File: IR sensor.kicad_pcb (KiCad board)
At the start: 2 copper layers, 33.5 x 16.8 mm, 23 parts, among them P1 BNC, P2 BNC, P3 BNC, P4 CONN_01X02, Q1 SOT-23-3 NPN, U1 TLV2770IDGKR, U2 LM311MX/NOPB

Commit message: ENH: Updates to IR sensors
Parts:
- removed D1: LED, Pin_Headers:Pin_Header_Straight_1x02
- removed P3: BNC, Pin_Headers:Pin_Header_Straight_1x02
- removed P4: CONN_01X02, Pin_Headers:Pin_Header_Straight_1x02
- removed the REF** at (142.0, 67.3)
- removed the REF** at (169.9, 78.5)
- removed RV1: POT, Pin_Headers:Pin_Header_Straight_1x03
- added REF**: 1pin, Connect:1pin, F.Cu at (172.2, 72.6)
- added REF**: 1pin, Connect:1pin, F.Cu at (140.7, 72.6)
- P1: value BNC -> CONN_01X08; footprint Pin_Headers:Pin_Header_Straight_1x02 -> Terminal_Blocks:TerminalBlock_Pheonix_MPT-2.54mm_8pol; moved to B.Cu
- P2: value BNC -> CONN_01X07; footprint Pin_Headers:Pin_Header_Straight_1x02 -> Terminal_Blocks:TerminalBlock_Pheonix_MPT-2.54mm_7pol; moved to B.Cu
- U1: value TLV2770IDGKR -> TLV2770
- U2: value LM311MX/NOPB -> LM311
- moved C1 12.3 mm to (165.4, 67.3), turned to 180 degrees
- moved P2 11.9 mm to (145.8, 67.1), turned to 0 degrees
- moved P1 9.40 mm to (163.6, 78.7), turned to 180 degrees
- moved R7 5.95 mm to (162.1, 75.7), turned to 0 degrees
- moved C5 4.36 mm to (164.5, 69.5), turned to 180 degrees
- moved R6 2.75 mm to (163.8, 72.9), turned to 90 degrees
- moved R1 2.54 mm to (157.2, 75.7), turned to 0 degrees
- moved Q1 1.83 mm to (166.4, 73.7), turned to 0 degrees
- moved R5 1.05 mm to (164.1, 71.1), turned to 180 degrees
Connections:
- C3 pad 1: Net-(C3-Pad1) -> IR+
- P1 pad 1: Net-(P1-Pad1) -> GND
- P1 pad 2: GND -> TTL+
- P2 pad 1: Net-(P2-Pad1) -> GND
- P2 pad 2: GND -> LED+
- Q1 pad 3: Net-(D1-Pad2) -> LED+
- R1 pad 2: Net-(P1-Pad1) -> E+
- R2 pad 2: Net-(P2-Pad1) -> S+
- R3 pad 2: Net-(P2-Pad1) -> S+
- R5 pad 2: Net-(P3-Pad1) -> TTL+
- R6 pad 2: Net-(P3-Pad1) -> TTL+
- U1 pad 2: Net-(C3-Pad1) -> IR+
- U1 pad 6: Net-(C3-Pad1) -> IR+
- U2 pad 2: Net-(C3-Pad1) -> IR+
- U2 pad 3: Net-(RV1-Pad2) -> POT2
- U2 pad 7: Net-(P3-Pad1) -> TTL+
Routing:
- net LED+: track 0.00 -> 27.9 mm
- net IR+: track 0.00 -> 23.4 mm
- net Net-(P3-Pad1): track 15.4 -> 0.00 mm
- net Net-(RV1-Pad2): track 13.6 -> 0.00 mm
- net TTL+: track 0.00 -> 12.1 mm
- net Net-(C3-Pad1): track 11.5 -> 0.00 mm
- net Net-(D1-Pad2): track 11.4 -> 0.00 mm
- net POT2: track 0.00 -> 10.7 mm
- net +5V: track 57.9 -> 49.6 mm
- net Net-(P2-Pad1): track 6.95 -> 0.00 mm
- net S+: track 0.00 -> 4.53 mm
- net E+: track 0.00 -> 4.03 mm
- net Net-(P1-Pad1): track 3.44 -> 0.00 mm
- net Net-(Q1-Pad2): track 2.16 -> 4.03 mm
- net Net-(Q1-Pad1): track 1.80 -> 2.35 mm
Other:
- board size 33.5 x 16.8 mm -> 36.6 x 16.8 mm
- board text added: "5V"
- board text added: "LED"
- board text added: "P1"
- board text added: "P2"
- board text added: "P3"
- board text removed: "POT"
- board text removed: "PWR"

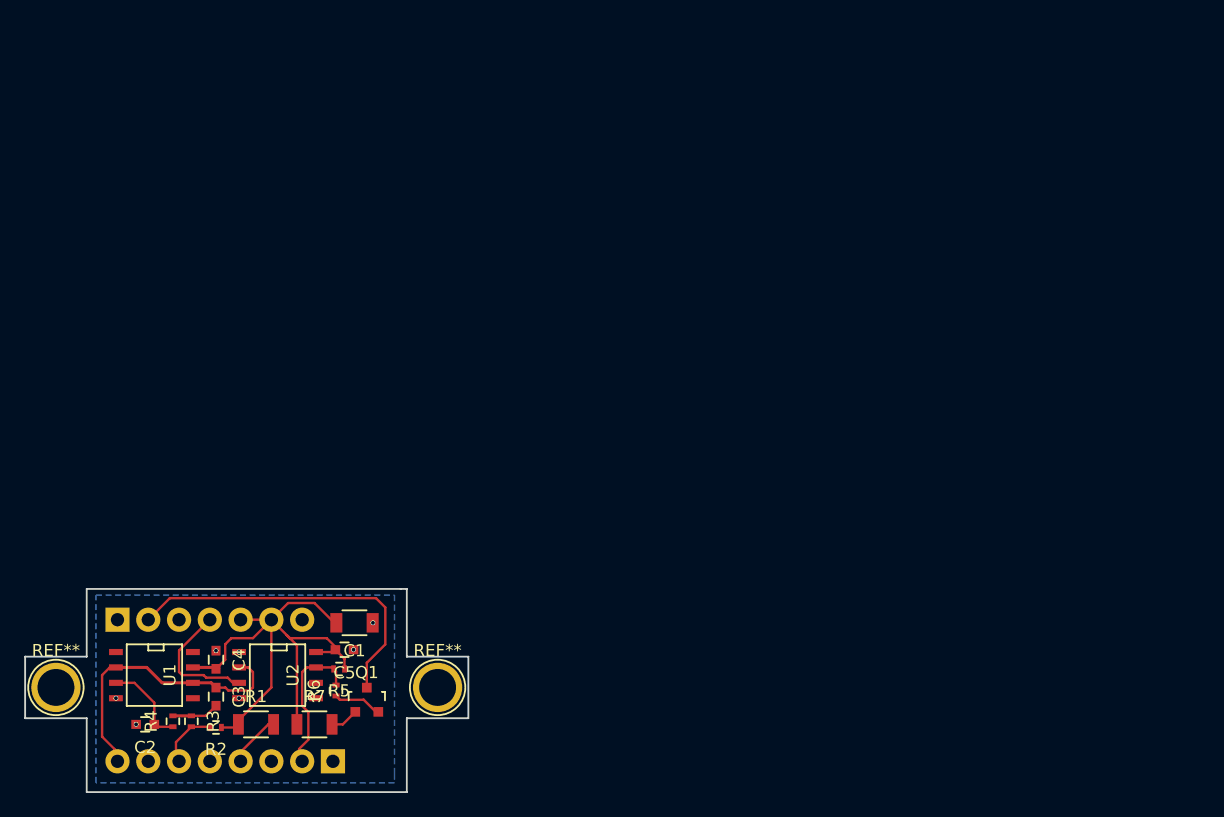
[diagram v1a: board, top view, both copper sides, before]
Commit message: ENH: Make PCB more compact
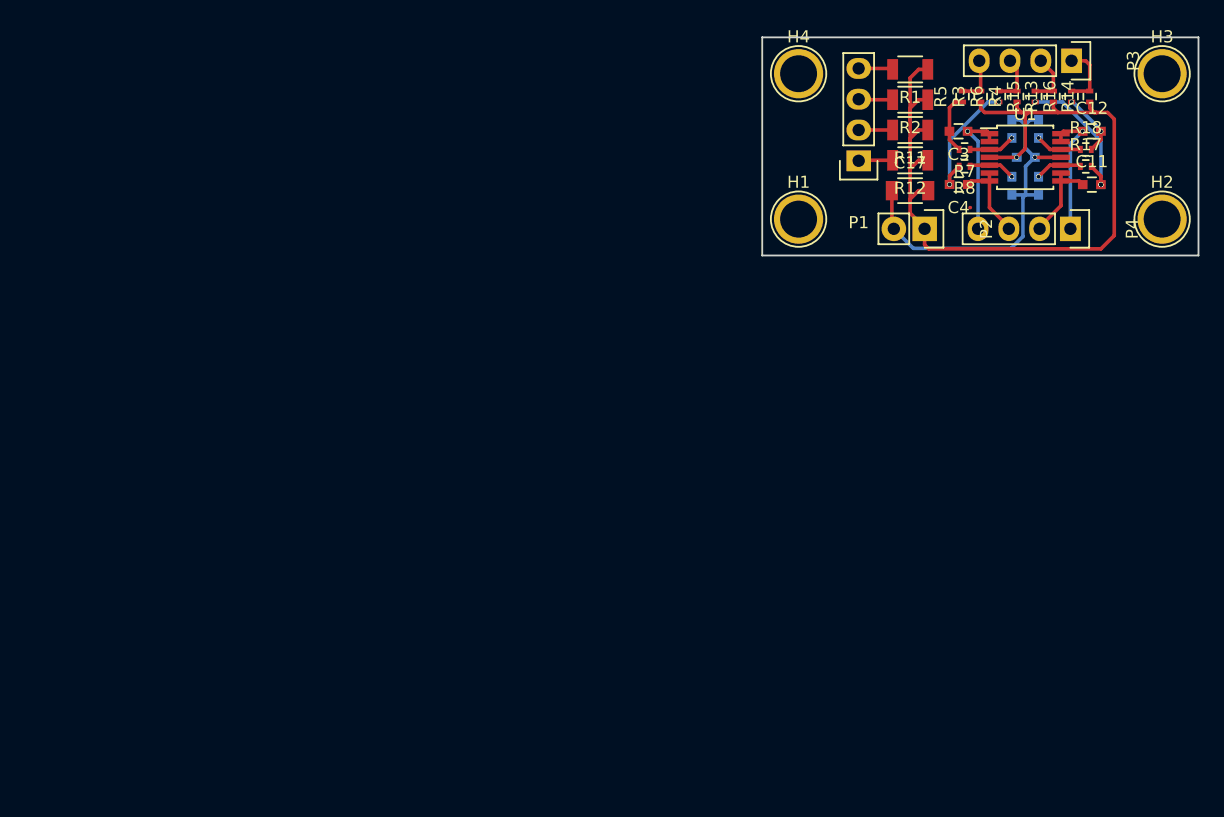
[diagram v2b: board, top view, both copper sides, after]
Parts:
- removed Q1: SOT-23-3 NPN, TO_SOT_Packages_SMD:SOT-23
- removed REF** (x2): 1pin, Connect:1pin
- removed U2: LM311, SMD_Packages:SOIC-8-N
- added C10: 0.1uF, Capacitors_SMD:C_0603, B.Cu at (221.8, 26.6)
- added C11: 0.1uF, Capacitors_SMD:C_0603, F.Cu at (226.2, 31.1)
- added C12: 0.1uF, Capacitors_SMD:C_0603, F.Cu at (226.2, 26.8)
- added C17: 10uF, Capacitors_SMD:C_1206, F.Cu at (211.2, 31.6)
- added C9: 0.1uF, Capacitors_SMD:C_0603, B.Cu at (221.8, 31.2)
- added H1: CONN_01X01, Connect:1pin, F.Cu at (202.0, 34.0)
- added H2: CONN_01X01, Connect:1pin, F.Cu at (232.0, 34.0)
- added H3: CONN_01X01, Connect:1pin, F.Cu at (232.0, 22.0)
- added H4: CONN_01X01, Connect:1pin, F.Cu at (202.0, 22.0)
- added P3: CONN_01X04, Pin_Headers:Pin_Header_Straight_1x04, F.Cu at (224.5, 20.9)
- added P4: CONN_01X04, Pin_Headers:Pin_Header_Straight_1x04, F.Cu at (224.4, 34.8)
- added R11: 100 0.25W, Resistors_SMD:R_1206, F.Cu at (211.2, 26.6)
- added R12: 100 0.25W, Resistors_SMD:R_1206, F.Cu at (211.2, 29.1)
- added R13: 10k, Resistors_SMD:R_0402, F.Cu at (223.0, 23.9)
- added R14: 10k, Resistors_SMD:R_0402, F.Cu at (226.0, 23.9)
- added R15: 10k, Resistors_SMD:R_0402, F.Cu at (221.5, 23.9)
- added R16: 10k, Resistors_SMD:R_0402, F.Cu at (224.5, 23.9)
- added R17: 10k, Resistors_SMD:R_0402, F.Cu at (225.7, 29.6)
- added R18: 10k, Resistors_SMD:R_0402, F.Cu at (225.7, 28.2)
- added R8: 10k, Resistors_SMD:R_0402, F.Cu at (215.7, 29.6)
- C1: value 10uF -> 0.1uF; footprint Capacitors_SMD:C_1206 -> Capacitors_SMD:C_0603; moved to B.Cu
- C2, C5: moved to B.Cu
- P1: value CONN_01X08 -> CONN_01X04; footprint Terminal_Blocks:TerminalBlock_Pheonix_MPT-2.54mm_8pol -> Pin_Headers:Pin_Header_Straight_1x04; moved to F.Cu
- P2: value CONN_01X07 -> CONN_01X02; footprint Terminal_Blocks:TerminalBlock_Pheonix_MPT-2.54mm_7pol -> Pin_Headers:Pin_Header_Straight_1x02; moved to F.Cu
- R2: value 10k -> 100 0.25W; footprint Resistors_SMD:R_0402 -> Resistors_SMD:R_1206
- R5: value 1k -> 10k
- R6: value 100k -> 10k
- R7: value 100 0.25W -> 10k; footprint Resistors_SMD:R_1206 -> Resistors_SMD:R_0402
- U1: value TLV2770 -> TLV2774; footprint SMD_Packages:SOIC-8-N -> Housings_SSOP:TSSOP-14_4.4x5mm_Pitch0.65mm
- moved R4 86.7 mm to (220.0, 23.9)
- moved C2 84.2 mm to (219.6, 31.2), turned to 270 degrees
- moved U1 83.6 mm to (220.7, 28.9), turned to 0 degrees
- moved R3 83.1 mm to (217.0, 23.9), turned to 90 degrees
- moved R2 77.2 mm to (211.2, 24.1)
- moved C3 77.0 mm to (215.2, 26.8), turned to 180 degrees
- moved R1 76.4 mm to (211.2, 21.6), turned to 180 degrees
- moved P2 74.0 mm to (212.4, 34.8), turned to 270 degrees
- moved R6 73.4 mm to (218.5, 23.9)
- moved C4 72.8 mm to (215.2, 31.1), turned to 180 degrees
- moved R7 71.6 mm to (215.7, 28.2), turned to 180 degrees
- moved R5 69.8 mm to (215.5, 23.9), turned to 90 degrees
- moved C5 69.4 mm to (220.8, 28.9)
- moved C1 67.9 mm to (219.6, 26.6), turned to 90 degrees
- moved P1 65.9 mm to (207.0, 29.2)
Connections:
- net E+ renamed E1+
- C1 pad 1: GND -> Net-(C1-Pad1)
- C1 pad 2: +5V -> GND
- C3 pad 1: IR+ -> O1
- C4 pad 1: GND -> O2
- C4 pad 2: +5V -> Net-(C4-Pad2)
- P1 pad 1: GND -> E4+
- P1 pad 2: TTL+ -> E3+
- P1 pad 3: GND -> E2+
- P2 pad 1: GND -> +5V
- P2 pad 2: LED+ -> GND
- R2 pad 2: S+ -> E2+
- R3 pad 1: Net-(C3-Pad2) -> +5V
- R3 pad 2: S+ -> S1+
- R4 pad 1: Net-(C2-Pad1) -> +5V
- R4 pad 2: Net-(C3-Pad2) -> S2+
- R5 pad 1: +5V -> Net-(C3-Pad2)
- R5 pad 2: TTL+ -> S1+
- R6 pad 1: Net-(Q1-Pad2) -> Net-(C4-Pad2)
- R6 pad 2: TTL+ -> S2+
- R7 pad 1: +5V -> Net-(C1-Pad1)
- R7 pad 2: Net-(Q1-Pad1) -> Net-(C3-Pad2)
- U1 pad 1: (no net) -> O1
- U1 pad 2: IR+ -> O1
- U1 pad 3: Net-(C2-Pad1) -> Net-(C1-Pad1)
- U1 pad 4: GND -> +5V
- U1 pad 5: (no net) -> Net-(C2-Pad1)
- U1 pad 6: IR+ -> O2
- U1 pad 7: +5V -> O2
- U1 pad 8: (no net) -> O3
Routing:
- net GND: track 0.32 -> 31.8 mm, vias 7 -> 1
- net LED+: track 27.9 -> 0.00 mm
- net IR+: track 23.4 -> 0.00 mm
- net +5V: track 49.6 -> 72.2 mm, vias 0 -> 1
- net Net-(C11-Pad2): track 0.00 -> 12.2 mm, vias 0 -> 3
- net TTL+: track 12.1 -> 0.00 mm
- net O4: track 0.00 -> 11.0 mm, vias 0 -> 1
- net O1: track 0.00 -> 11.0 mm, vias 0 -> 1
- net Net-(C4-Pad2): track 0.00 -> 10.8 mm, vias 0 -> 2
- net POT2: track 10.7 -> 0.00 mm
- net O3: track 0.00 -> 7.28 mm
- net O2: track 0.00 -> 7.17 mm
- net Net-(C12-Pad2): track 0.00 -> 5.31 mm, vias 0 -> 2
- net S4+: track 0.00 -> 5.30 mm
- net S+: track 4.53 -> 0.00 mm
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- removed copper zone on B.Cu, net GND
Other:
- board size 36.6 x 16.8 mm -> 36 x 18 mm
- net class Default: clearance 0.2 -> 0.15; trace_width 0.2 -> 0.3
- rule trace_clearance: 0.2 -> 0.15
- board text removed: "5V"
- board text removed: "E"
- board text removed: "IR"
- board text removed: "LED"
- board text removed: "P1"
- board text removed: "P2"
- board text removed: "P3"
- board text removed: "S"
- board text removed: "TTL"
- board text removed: "⏚"

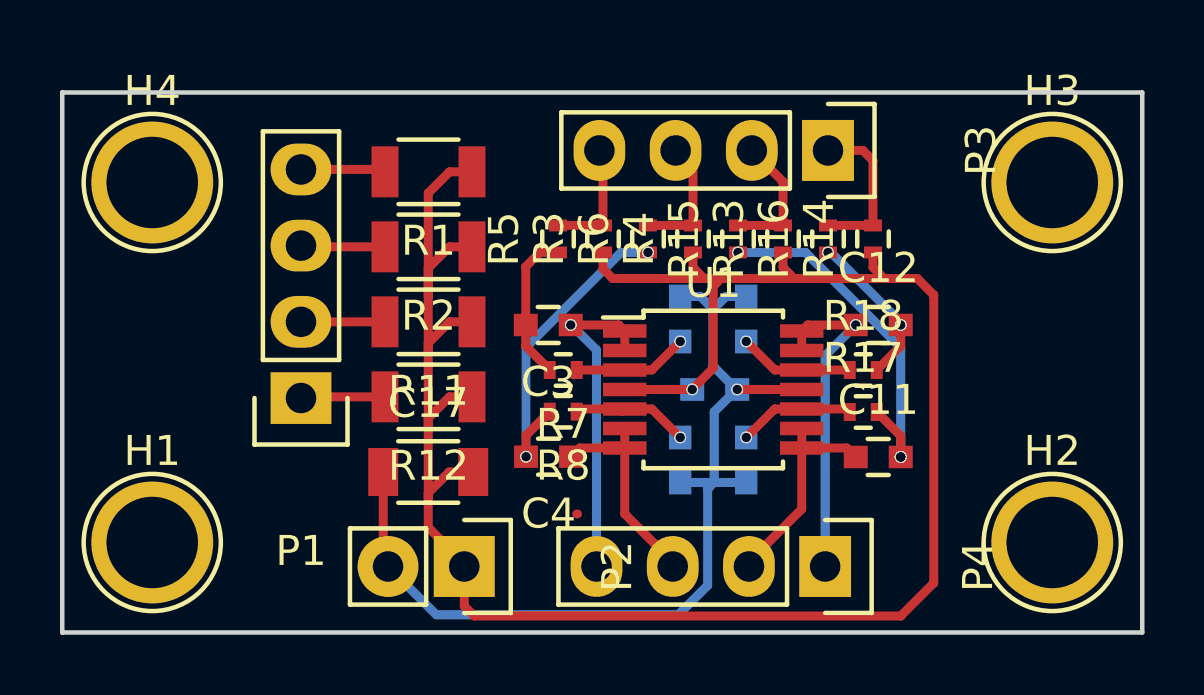
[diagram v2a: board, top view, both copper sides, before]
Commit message: Update to KiCAD 5
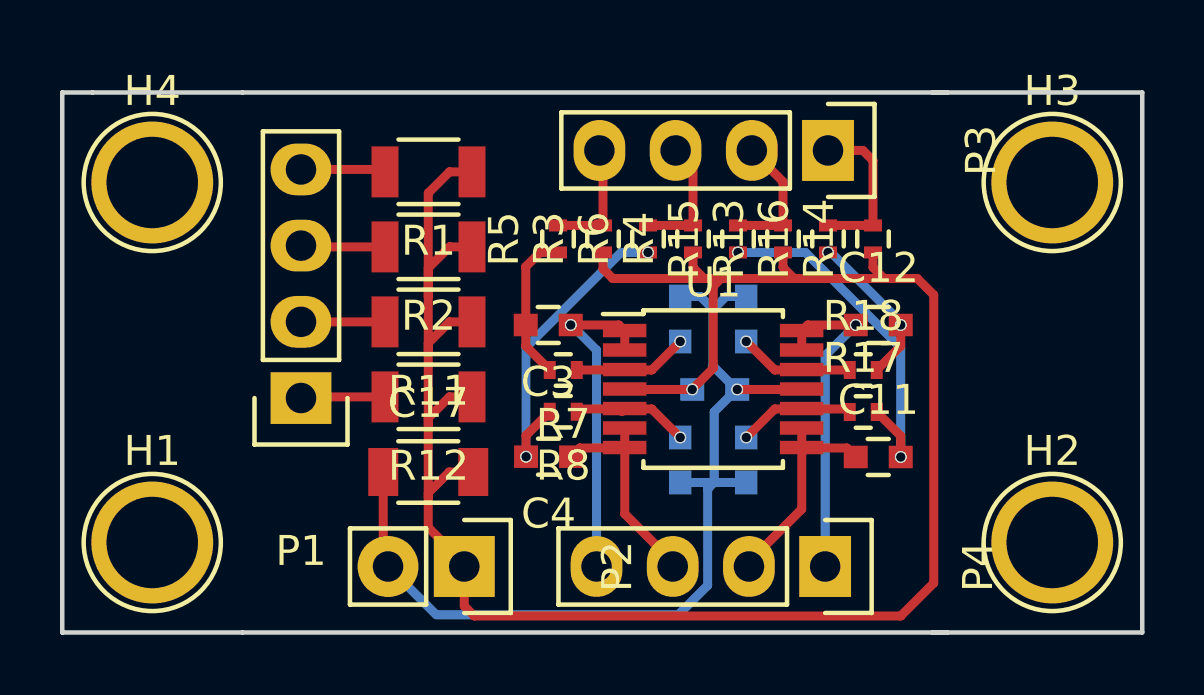
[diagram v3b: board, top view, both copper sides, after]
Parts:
- U1: value TLV2774 -> LM2902; footprint Housings_SSOP:TSSOP-14_4.4x5mm_Pitch0.65mm -> Package_SO:TSSOP-14_4.4x5mm_P0.65mm
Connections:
- H1 pad 1: Net-(H1-Pad1) -> (no net)
- H2 pad 1: Net-(H2-Pad1) -> (no net)
- H3 pad 1: Net-(H3-Pad1) -> (no net)
- H4 pad 1: Net-(H4-Pad1) -> (no net)
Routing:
- net Net-(C11-Pad2): vias 3 -> 2
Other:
- outline, holes or cut-outs redrawn
